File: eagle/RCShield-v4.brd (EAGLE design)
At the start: 92.7 x 82.5 mm, 66 parts, among them J1/J2 JOYSTICKPTH, P1/P3 POT, P2/P4 POT, U1 TOUSCRUINO_SHIELD, U2 FT232RL-BASICSSOP, U3 TS5A3157DBV, U4 XBEE, U5 TS5A3157DBV, U6 TS5A3157DBV, U7 TS5A3157DBV, U8 TS5A3157DBV, X1 USB

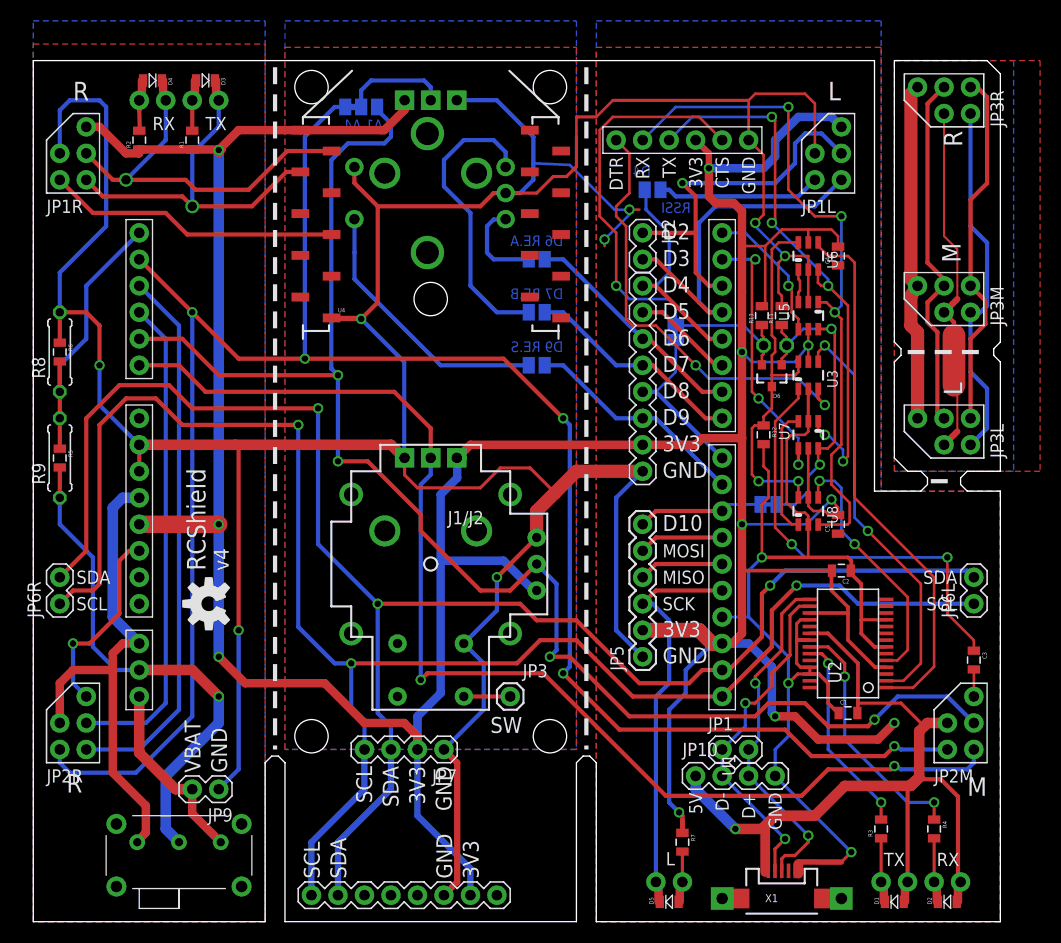
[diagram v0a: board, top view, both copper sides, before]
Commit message: 
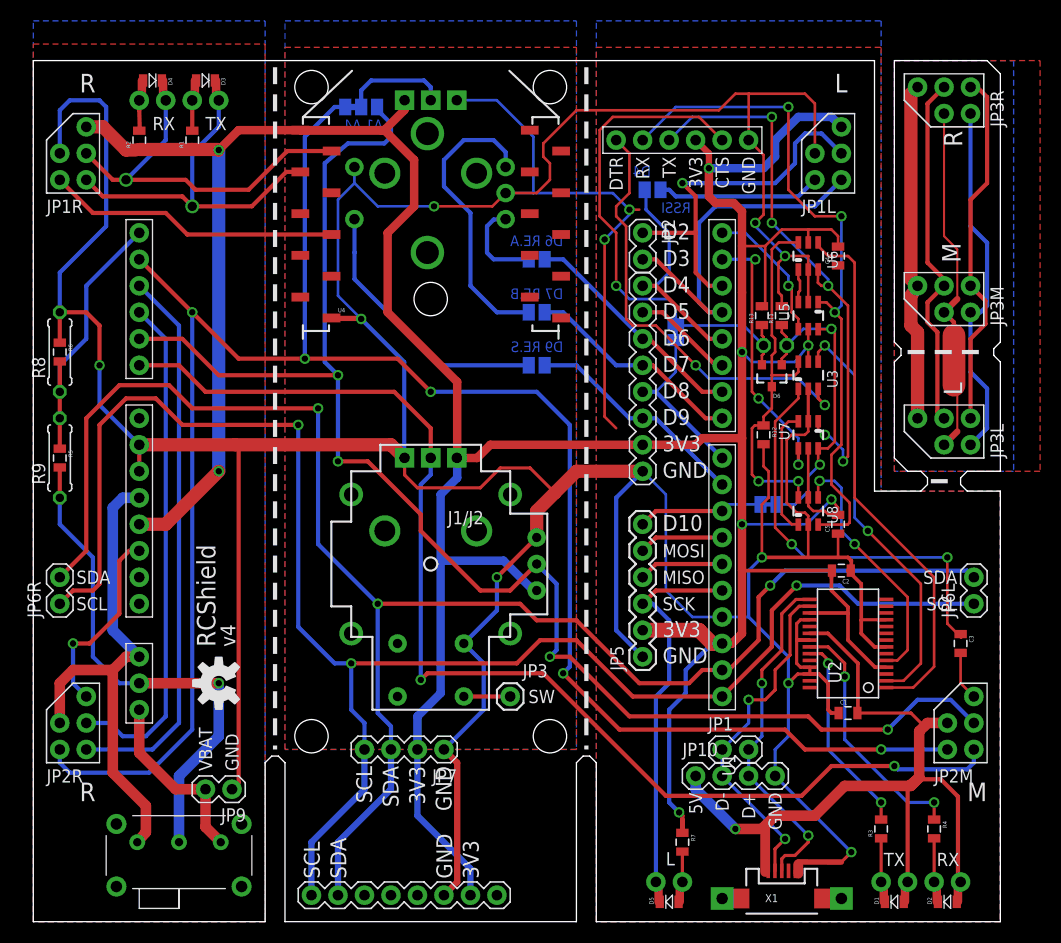
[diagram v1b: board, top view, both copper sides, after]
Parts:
- moved U$1 7.68 mm to (17.8, 22.9)
- moved C3 2.03 mm to (88.9, 26.7)
- moved JP9 1.27 mm to (19.1, 12.7)
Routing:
- net GND: track 473.5 -> 515.9 mm
- net 3.3V: track 396.8 -> 377.2 mm, vias 11 -> 8
- net N$1: track 2.59 -> 4.71 mm
- net A2: track 46.9 -> 48.7 mm
- net DTR: track 41.9 -> 40.5 mm
- net A3: track 52.7 -> 53.4 mm
- net VBAT: track 18.1 -> 17.6 mm
